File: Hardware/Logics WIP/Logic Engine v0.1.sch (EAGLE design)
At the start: 33 parts, among them IC1 MEGA328P, J2 2.1MMJACK, X1 16MHz

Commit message: Need to repackage inductor on Logic Engine to include GND (duh!)
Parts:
- removed D3: Green, minimidi:LEDCHIPLED_1206
- removed J2: 2.1MMJACK, minimidi:2.1MMJACK
- removed R4: 1.0 K, minimidi:R-US_M1206
- removed U$1: ROYAL-ENGINEERS-OF-NABOOSMALL, rseries:ROYAL-ENGINEERS-OF-NABOOSMALL
- removed X1: 16MHz, digg:CERMOSCILL
- added D1: (no value), minimidi:LEDCHIPLED_1206
- added F1: (no value), adafruit:PTCFUSE-1812
- added R2: 1K, adafruit:R-US_R0805
- added Y1: 16MHz, SparkFun-FreqCtrl:RESONATOR16MHZ
- C1: device minimidi:C-USC1206K -> adafruit:C-USC0805K
- CIN: device adafruit:C-USC0805K -> adafruit:C-USC1206
- D2: value (none) -> Green
- R1: value 10k -> 1K
- R3: value 1.0 K -> 10k; device minimidi:R-US_M1206 -> adafruit:R-US_R0805
- renumbered C2 to C3, JP7 to JP1
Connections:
- new net N$10: F1.2, PWR_SEL1.2
- net +5V: now also F1.1, R3.2; no longer PWR_SEL1.2, R4.1
- net GND: now also D1.C, Y1.2; no longer D3.C, X1.GND
- net N$1: now also Y1.1; no longer X1.IN
- net N$2: now also Y1.3; no longer X1.OUT
- net N$4: now also D2.A, R2.2; no longer D3.A, R3.2
- net N$5: now also D1.A, R1.1; no longer D2.A, R4.2
- net RST: now also R3.1; no longer R1.1
- net SCK: now also R2.1; no longer R3.1
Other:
- moved on the sheet: C1, CIN, CINX, D2, R1, R3

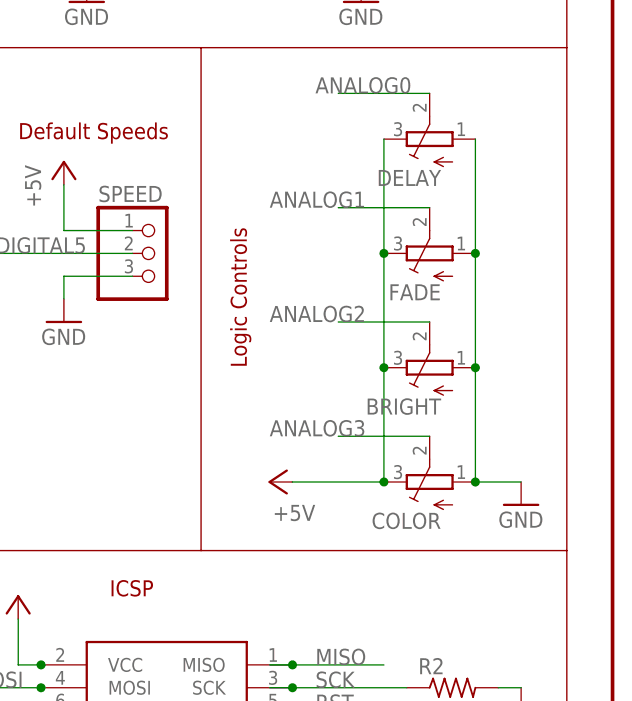
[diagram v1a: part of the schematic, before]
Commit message: 
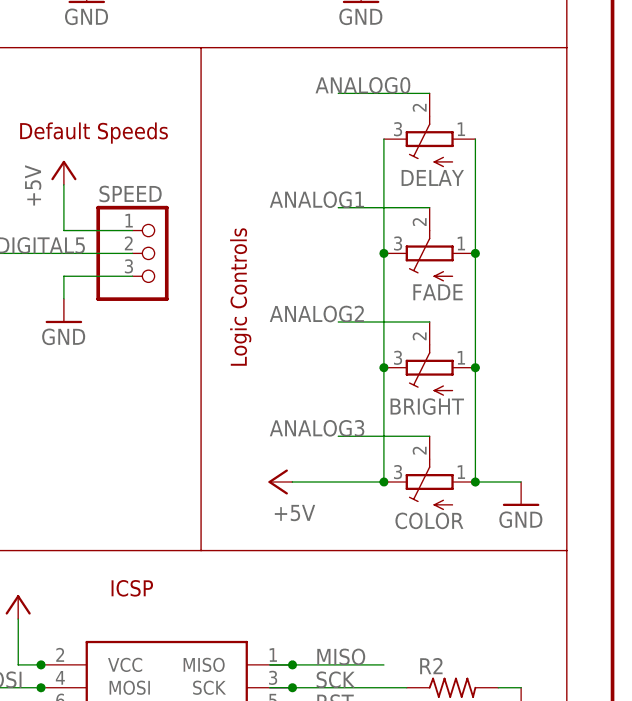
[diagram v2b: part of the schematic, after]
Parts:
- BRIGHT, COLOR, DELAY, FADE: device adafruit:TRIMPOTTC33X -> rseries:TRIMPOT3364W
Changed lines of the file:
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@@
 <part name="P+5" library="supply1" deviceset="+5V" device=""/>
 <part name="GND6" library="supply1" deviceset="GND" device=""/>
-<part name="DELAY" library="adafruit" deviceset="TRIMPOT" device="TC33X"/>
 <part name="SPEED" library="pinhead" deviceset="PINHD-1X3" device=""/>
 <part name="P+3" library="supply1" deviceset="+5V" device=""/>
 <part name="GND3" library="supply1" deviceset="GND" device=""/>
-<part name="FADE" library="adafruit" deviceset="TRIMPOT" device="TC33X"/>
-<part name="BRIGHT" library="adafruit" deviceset="TRIMPOT" device="TC33X"/>
-<part name="COLOR" library="adafruit" deviceset="TRIMPOT" device="TC33X"/>
 <part name="GND7" library="supply1" deviceset="GND" device=""/>
 <part name="P+7" library="supply1" deviceset="+5V" device=""/>
@@
 <part name="C1" library="adafruit" deviceset="C-US" device="C0805K" value="0.1uF"/>
 <part name="F1" library="adafruit" deviceset="PTCFUSE" device="-1812"/>
+<part name="DELAY" library="rseries" deviceset="TRIMPOT" device="3364W"/>
+<part name="FADE" library="rseries" deviceset="TRIMPOT" device="3364W"/>
+<part name="BRIGHT" library="rseries" deviceset="TRIMPOT" device="3364W"/>
+<part name="COLOR" library="rseries" deviceset="TRIMPOT" device="3364W"/>
 </parts>
 <sheets>
@@
 <instance part="P+5" gate="1" x="220.98" y="147.32"/>
 <instance part="GND6" gate="1" x="220.98" y="129.54"/>
-<instance part="DELAY" gate="G$1" x="228.6" y="114.3" smashed="yes" rot="R90">
-<attribute name="NAME" x="229.87" y="110.871" size="1.778" layer="95" rot="R180"/>
-<attribute name="VALUE" x="232.41" y="110.49" size="1.778" layer="96" rot="R180"/>
-</instance>
 <instance part="SPEED" gate="A" x="198.12" y="101.6"/>
 <instance part="P+3" gate="1" x="187.96" y="111.76"/>
 <instance part="GND3" gate="1" x="187.96" y="93.98"/>
-<instance part="FADE" gate="G$1" x="228.6" y="101.6" smashed="yes" rot="R90">
-<attribute name="NAME" x="229.87" y="98.171" size="1.778" layer="95" rot="R180"/>
-<attribute name="VALUE" x="232.41" y="97.79" size="1.778" layer="96" rot="R180"/>
-</instance>
-<instance part="BRIGHT" gate="G$1" x="228.6" y="88.9" smashed="yes" rot="R90">
-<attribute name="NAME" x="229.87" y="85.471" size="1.778" layer="95" rot="R180"/>
-<attribute name="VALUE" x="232.41" y="85.09" size="1.778" layer="96" rot="R180"/>
-</instance>
-<instance part="COLOR" gate="G$1" x="228.6" y="76.2" smashed="yes" rot="R90">
-<attribute name="NAME" x="229.87" y="72.771" size="1.778" layer="95" rot="R180"/>
-<attribute name="VALUE" x="232.41" y="72.39" size="1.778" layer="96" rot="R180"/>
-</instance>
 <instance part="GND7" gate="1" x="238.76" y="73.66"/>
 <instance part="P+7" gate="1" x="210.82" y="76.2" rot="R90"/>
@@
 <instance part="C1" gate="G$1" x="152.4" y="93.98"/>
 <instance part="F1" gate="G$1" x="147.32" y="119.38"/>
+<instance part="DELAY" gate="G$1" x="228.6" y="114.3" smashed="yes" rot="R90">
+<attribute name="NAME" x="232.41" y="110.871" size="1.778" layer="95" rot="R180"/>
+<attribute name="VALUE" x="232.41" y="110.49" size="1.778" layer="96" rot="R180"/>
+</instance>
+<instance part="FADE" gate="G$1" x="228.6" y="101.6" smashed="yes" rot="R90">
+<attribute name="NAME" x="232.41" y="98.171" size="1.778" layer="95" rot="R180"/>
+<attribute name="VALUE" x="232.41" y="97.79" size="1.778" layer="96" rot="R180"/>
+</instance>
+<instance part="BRIGHT" gate="G$1" x="228.6" y="88.9" smashed="yes" rot="R90">
+<attribute name="NAME" x="232.41" y="85.471" size="1.778" layer="95" rot="R180"/>
+<attribute name="VALUE" x="232.41" y="85.09" size="1.778" layer="96" rot="R180"/>
+</instance>
+<instance part="COLOR" gate="G$1" x="228.6" y="76.2" smashed="yes" rot="R90">
+<attribute name="NAME" x="232.41" y="72.771" size="1.778" layer="95" rot="R180"/>
+<attribute name="VALUE" x="232.41" y="72.39" size="1.778" layer="96" rot="R180"/>
+</instance>
 </instances>
 <busses>
@@
 </segment>
 <segment>
+<wire x1="233.68" y1="114.3" x2="233.68" y2="101.6" width="0.1524" layer="91"/>
+<wire x1="233.68" y1="101.6" x2="233.68" y2="88.9" width="0.1524" layer="91"/>
+<pinref part="GND7" gate="1" pin="GND"/>
+<wire x1="233.68" y1="88.9" x2="233.68" y2="76.2" width="0.1524" layer="91"/>
+<wire x1="233.68" y1="76.2" x2="238.76" y2="76.2" width="0.1524" layer="91"/>
 <pinref part="DELAY" gate="G$1" pin="A"/>
 <pinref part="FADE" gate="G$1" pin="A"/>
-<wire x1="233.68" y1="114.3" x2="233.68" y2="101.6" width="0.1524" layer="91"/>
+<junction x="233.68" y="101.6"/>
 <pinref part="BRIGHT" gate="G$1" pin="A"/>
-<wire x1="233.68" y1="101.6" x2="233.68" y2="88.9" width="0.1524" layer="91"/>
-<junction x="233.68" y="101.6"/>
+<junction x="233.68" y="88.9"/>
 <pinref part="COLOR" gate="G$1" pin="A"/>
-<wire x1="233.68" y1="88.9" x2="233.68" y2="76.2" width="0.1524" layer="91"/>
-<junction x="233.68" y="88.9"/>
 <junction x="233.68" y="76.2"/>
-<pinref part="GND7" gate="1" pin="GND"/>
-<wire x1="233.68" y1="76.2" x2="238.76" y2="76.2" width="0.1524" layer="91"/>
 </segment>
 <segment>
@@
 </segment>
 <segment>
+<wire x1="223.52" y1="114.3" x2="223.52" y2="101.6" width="0.1524" layer="91"/>
+<wire x1="223.52" y1="101.6" x2="223.52" y2="88.9" width="0.1524" layer="91"/>
+<pinref part="P+7" gate="1" pin="+5V"/>
+<wire x1="223.52" y1="88.9" x2="223.52" y2="76.2" width="0.1524" layer="91"/>
+<wire x1="223.52" y1="76.2" x2="213.36" y2="76.2" width="0.1524" layer="91"/>
 <pinref part="DELAY" gate="G$1" pin="E"/>
 <pinref part="FADE" gate="G$1" pin="E"/>
-<wire x1="223.52" y1="114.3" x2="223.52" y2="101.6" width="0.1524" layer="91"/>
+<junction x="223.52" y="101.6"/>
 <pinref part="BRIGHT" gate="G$1" pin="E"/>
-<wire x1="223.52" y1="101.6" x2="223.52" y2="88.9" width="0.1524" layer="91"/>
-<junction x="223.52" y="101.6"/>
+<junction x="223.52" y="88.9"/>
 <pinref part="COLOR" gate="G$1" pin="E"/>
-<wire x1="223.52" y1="88.9" x2="223.52" y2="76.2" width="0.1524" layer="91"/>
-<junction x="223.52" y="88.9"/>
 <junction x="223.52" y="76.2"/>
-<pinref part="P+7" gate="1" pin="+5V"/>
-<wire x1="223.52" y1="76.2" x2="213.36" y2="76.2" width="0.1524" layer="91"/>
 </segment>
 <segment>
@@
 </segment>
 <segment>
-<pinref part="DELAY" gate="G$1" pin="S"/>
 <wire x1="228.6" y1="119.38" x2="218.44" y2="119.38" width="0.1524" layer="91"/>
 <label x="215.9" y="119.38" size="1.778" layer="95"/>
+<pinref part="DELAY" gate="G$1" pin="S"/>
 </segment>
 </net>
@@
 </segment>
 <segment>
-<pinref part="FADE" gate="G$1" pin="S"/>
 <wire x1="228.6" y1="106.68" x2="218.44" y2="106.68" width="0.1524" layer="91"/>
 <label x="210.82" y="106.68" size="1.778" layer="95"/>
+<pinref part="FADE" gate="G$1" pin="S"/>
 </segment>
 </net>
@@
 </segment>
 <segment>
-<pinref part="BRIGHT" gate="G$1" pin="S"/>
 <wire x1="228.6" y1="93.98" x2="218.44" y2="93.98" width="0.1524" layer="91"/>
 <label x="210.82" y="93.98" size="1.778" layer="95"/>
+<pinref part="BRIGHT" gate="G$1" pin="S"/>
 </segment>
 </net>
@@
 </segment>
 <segment>
-<pinref part="COLOR" gate="G$1" pin="S"/>
 <wire x1="228.6" y1="81.28" x2="218.44" y2="81.28" width="0.1524" layer="91"/>
 <label x="210.82" y="81.28" size="1.778" layer="95"/>
-</segment>
-</net>
+<pinref part="COLOR" gate="G$1" pin="S"/>
+</segment>
+</net>
